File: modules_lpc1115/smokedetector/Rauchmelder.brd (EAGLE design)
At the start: 38 x 65 mm, 75 parts, among them IC1 BD9G101, IC2 LPC1115, Q1 BC856, Q3 BCP52, Q4 ASFL, T1 BC847C, T2 BC817

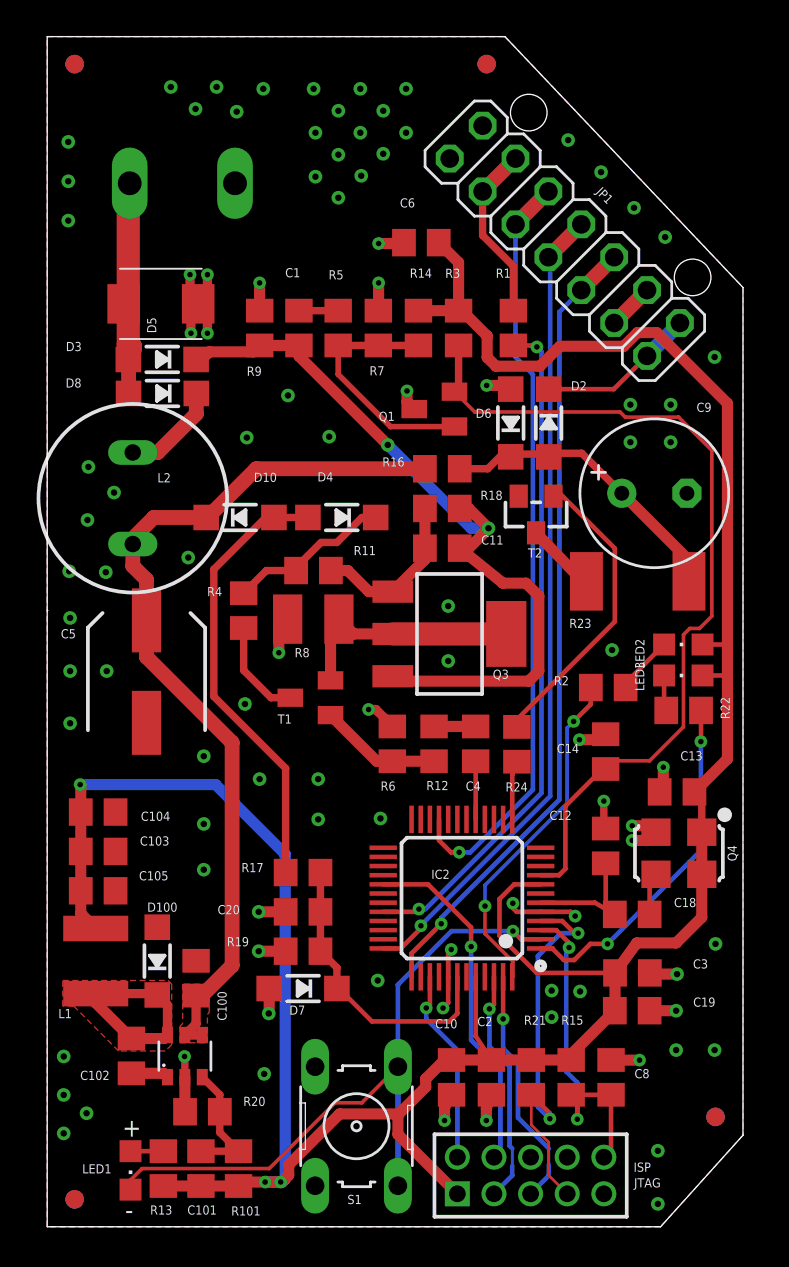
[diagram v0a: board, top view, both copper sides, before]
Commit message: [RM] - solved SWD connector collision with button
and optimized silk screen 
turned 330uF capacitor so that it is the same way rotated as in older PCB versions
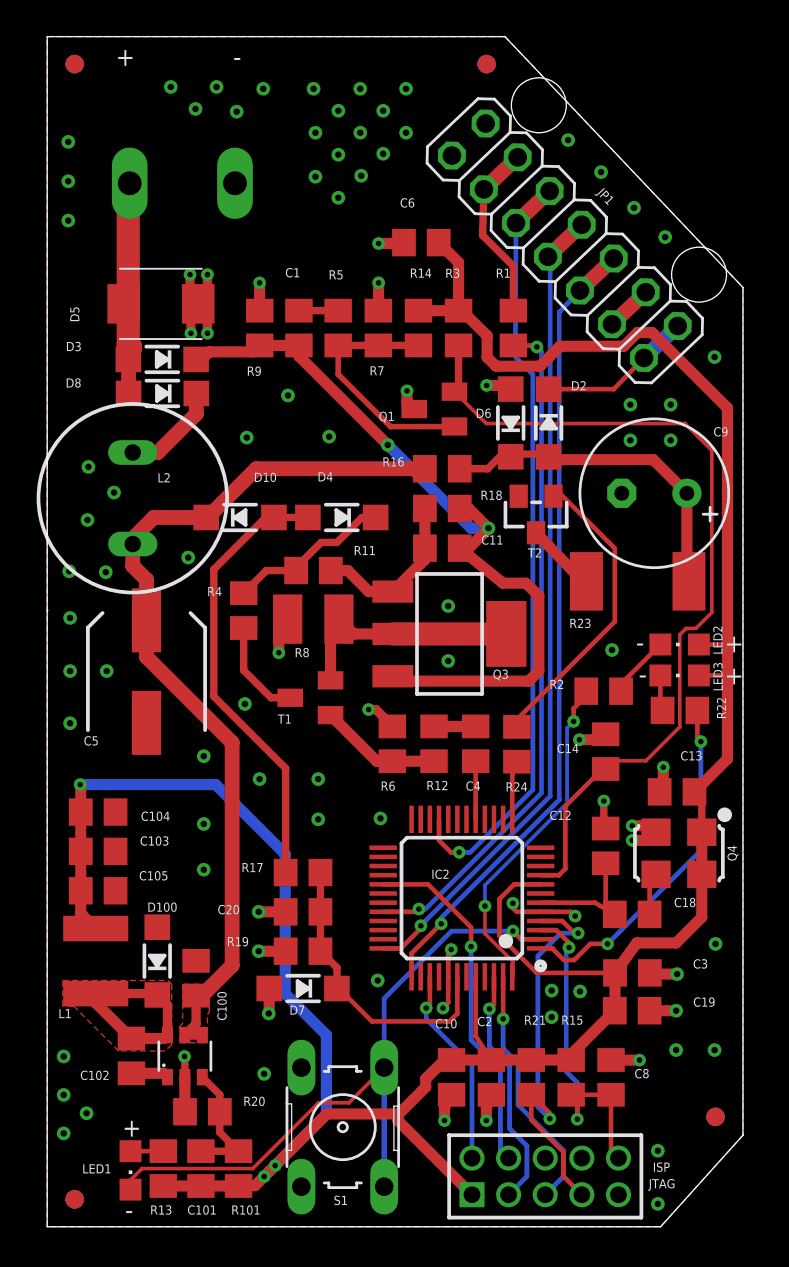
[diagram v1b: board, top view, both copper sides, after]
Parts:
- moved JTAG 0.80 mm to (27.2, 2.75)
- moved S1 0.75 mm to (16.1, 5.44)
- moved R2 0.32 mm to (30.4, 29.2)
- moved LED2 0.20 mm to (34.5, 31.8)
- moved LED3 0.20 mm to (34.5, 30.1)
- moved R22 0.20 mm to (34.6, 28.2)
- turned C9 to 180 degrees
- turned JP1 to 133.5 degrees
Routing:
- net N$10: track 16.7 -> 18.7 mm
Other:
- board text added: "Selfbus RM-ARM v3.8.4 RC2"
- board text removed: "Selfbus RM-ARM v3.8.4 RC1"

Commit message: [RM] -  smaller positioning changes; increased version
set version from 3.8.x to 3.9.x because of switch to 0805 which is a quite big change
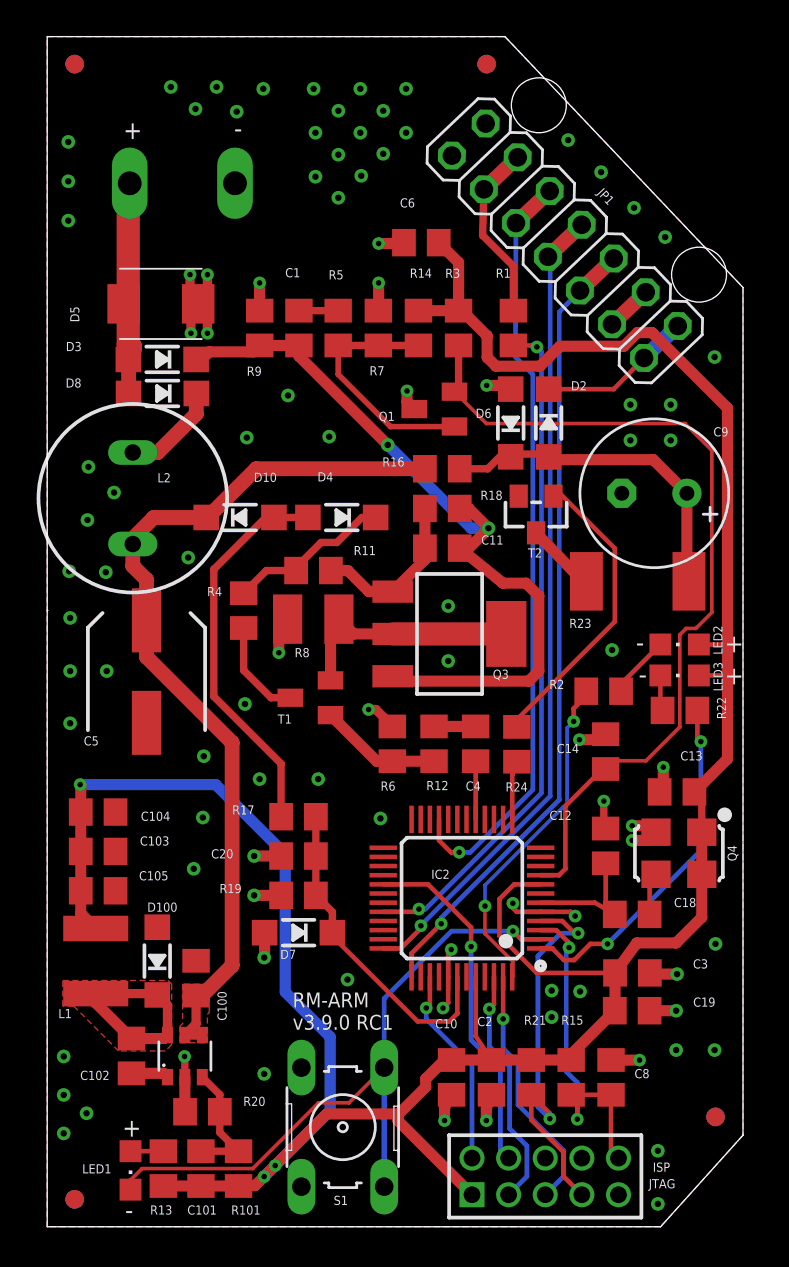
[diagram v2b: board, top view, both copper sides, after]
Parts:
- moved C20 3.06 mm to (13.7, 20.2)
- moved R17 3.06 mm to (13.7, 22.4)
- moved D7 3.06 mm to (13.7, 16.1)
- moved R19 3.06 mm to (13.7, 18.1)
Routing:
- net REF: track 24.5 -> 21.3 mm
- net BUS_V1: track 16.2 -> 17.8 mm
- net GND: vias 97 -> 96
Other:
- board text added: "RM-ARM v3.9.0 RC1"
- board text added: "Selfbus RM-ARM v3.9.0 RC1"
- board text removed: "Selfbus RM-ARM v3.8.4 RC2"

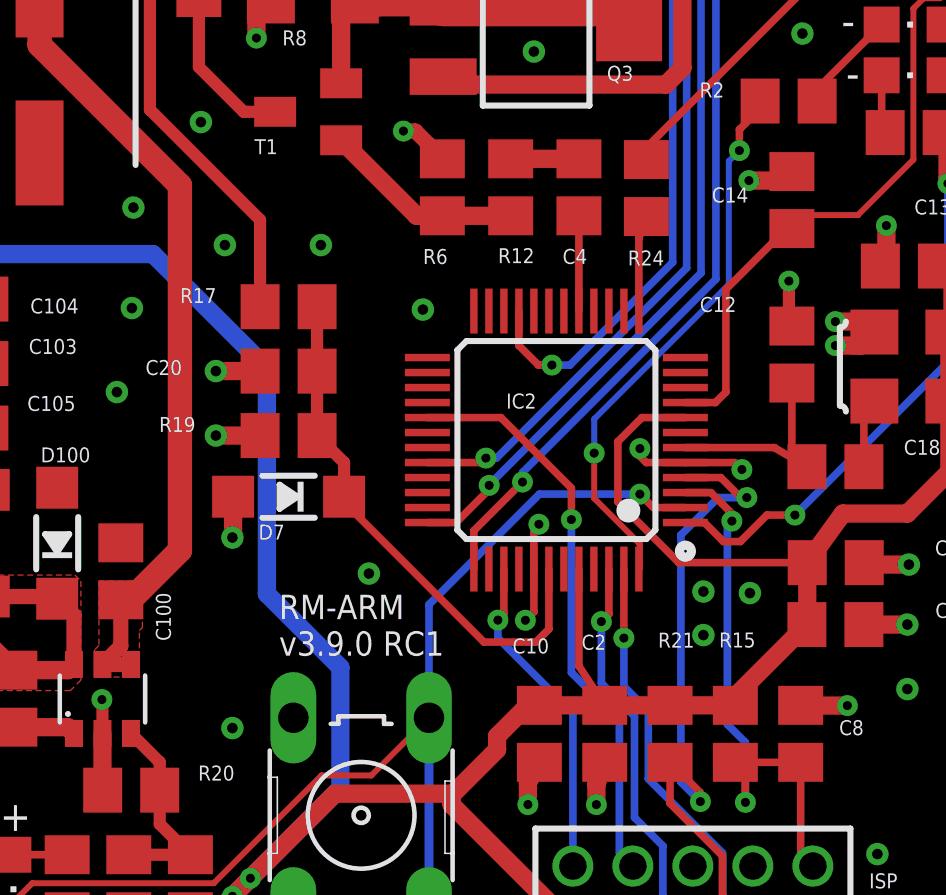
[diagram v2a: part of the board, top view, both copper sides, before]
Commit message: [RM] - corrected wrong part for C102 and error in solder topcoat
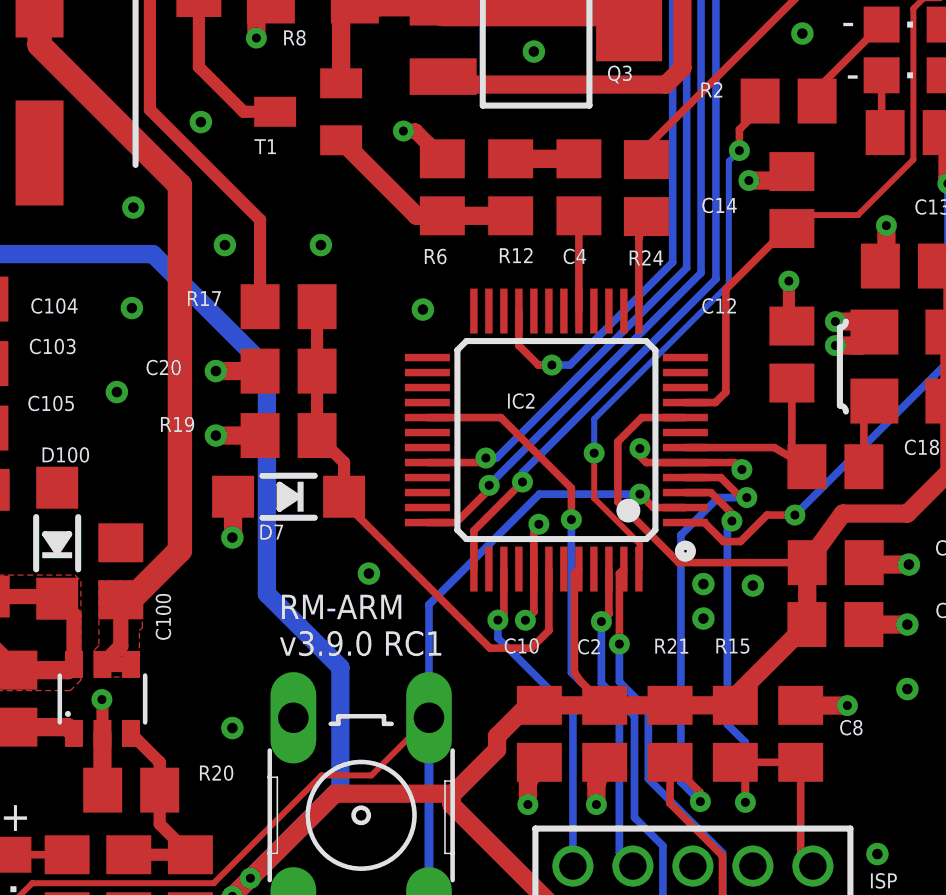
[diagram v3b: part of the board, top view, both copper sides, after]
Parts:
- C102: device rcl:R0805 -> rcl:C0805

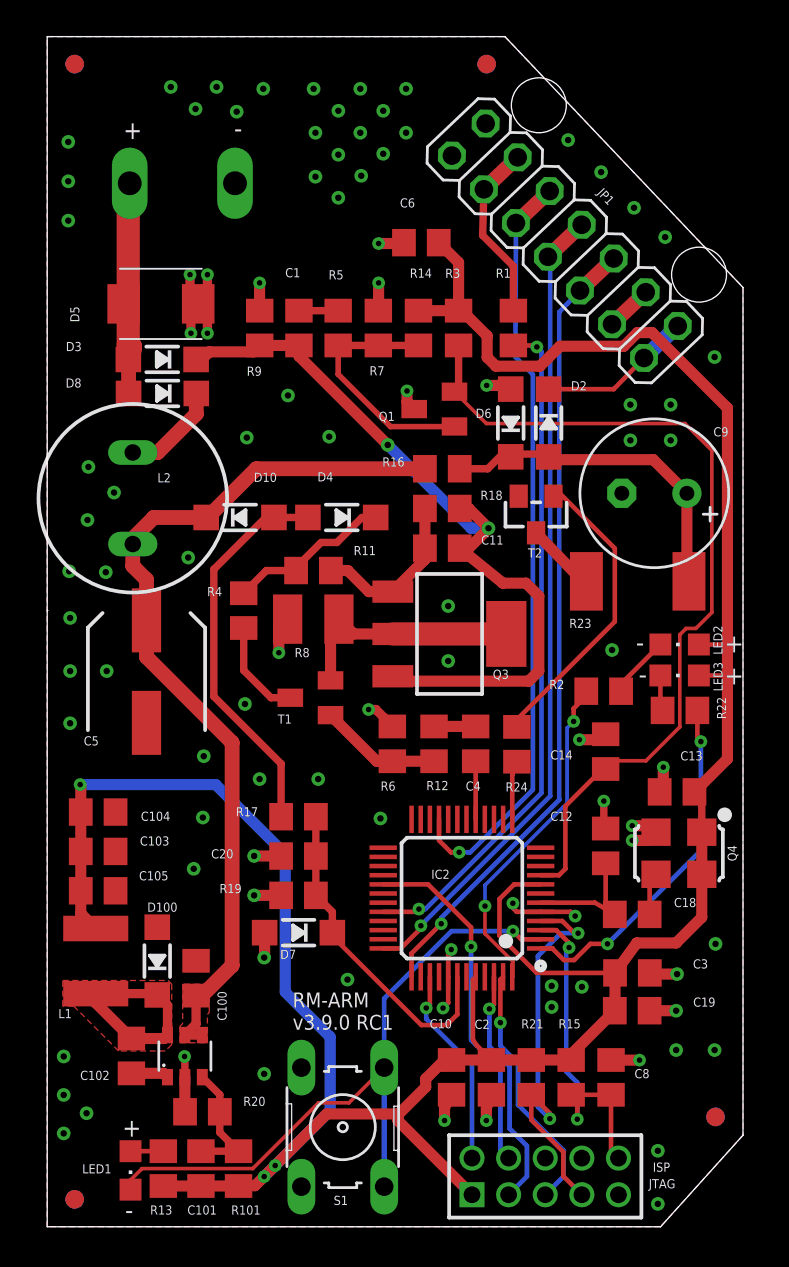
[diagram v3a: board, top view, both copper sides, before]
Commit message: [RM] - optimized silk screen; renamed pwr parts to correspond ARM TS
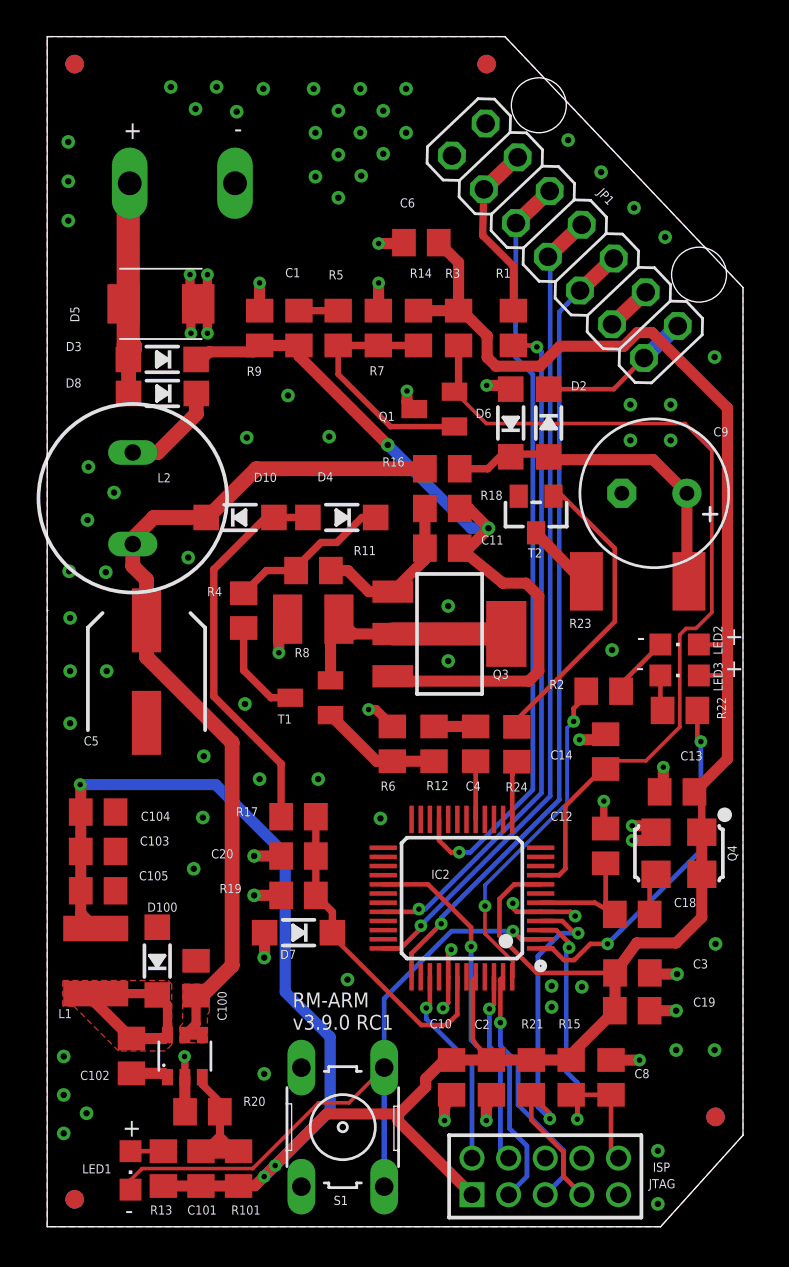
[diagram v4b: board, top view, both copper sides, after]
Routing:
- net FB1: track 6.92 -> 9.76 mm
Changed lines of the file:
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@@
 <text x="4.1512" y="59.403575" size="1" layer="21" ratio="10">+</text>
 <text x="10.2012" y="59.495575" size="1.016" layer="21" ratio="10">-</text>
-<text x="37.0012" y="31.370575" size="1" layer="21" ratio="10">+</text>
-<text x="37.0012" y="29.620575" size="1" layer="21" ratio="10">+</text>
-<text x="32.1512" y="31.420575" size="1.016" layer="21" ratio="10">-</text>
-<text x="32.3012" y="29.670575" size="1.016" layer="21" ratio="10">-</text>
+<text x="37.0012" y="31.770575" size="1" layer="21" ratio="10">+</text>
+<text x="37.0012" y="30.020575" size="1" layer="21" ratio="10">+</text>
+<text x="32.2012" y="31.720575" size="1.016" layer="21" ratio="10">-</text>
+<text x="32.1512" y="30.070575" size="1.016" layer="21" ratio="10">-</text>
 <text x="13.404375" y="10.7619" size="0.8128" layer="21" ratio="7">RM-ARM
 v3.9.0 RC1</text>
@@
 <contactref element="R20" pad="2"/>
 <contactref element="R101" pad="1"/>
-<wire x1="8.469" y1="8.17" x2="9.427" y2="7.212" width="0.4064" layer="1"/>
-<wire x1="9.427" y1="7.212" x2="9.427" y2="6.28" width="0.4064" layer="1"/>
-<wire x1="8.396" y1="4.1274125" x2="10.45" y2="4.1274125" width="0.4064" layer="1"/>
-<wire x1="10.45" y1="4.1274125" x2="9.427" y2="5.1504125" width="0.4064" layer="1"/>
-<wire x1="9.427" y1="5.1504125" x2="9.427" y2="6.28" width="0.4064" layer="1"/>
+<wire x1="9.427" y1="6.812" x2="8.469" y2="7.77" width="0.4064" layer="1"/>
+<wire x1="8.469" y1="8.17" x2="8.469" y2="7.77" width="0.4064" layer="1"/>
+<wire x1="9.427" y1="6.812" x2="9.427" y2="6.28" width="0.4064" layer="1"/>
+<wire x1="10.35" y1="4.2274125" x2="8.496" y2="4.2274125" width="1.016" layer="1"/>
+<wire x1="8.396" y1="4.1274125" x2="8.496" y2="4.2274125" width="1.016" layer="1"/>
+<wire x1="10.35" y1="4.2274125" x2="10.45" y2="4.1274125" width="1.016" layer="1"/>
+<wire x1="10.45" y1="4.1274125" x2="10.3" y2="4.1274125" width="0.4064" layer="1"/>
+<wire x1="10.3" y1="4.1274125" x2="9.427" y2="5.0004125" width="0.4064" layer="1"/>
+<wire x1="9.427" y1="5.0004125" x2="9.427" y2="6.28" width="0.4064" layer="1"/>
+<wire x1="9.427" y1="6.28" x2="9.427" y2="5.0084125" width="0.4064" layer="1"/>
+<wire x1="9.427" y1="5.0084125" x2="8.546" y2="4.1274125" width="0.4064" layer="1"/>
+<wire x1="8.546" y1="4.1274125" x2="8.396" y2="4.1274125" width="0.4064" layer="1"/>
 </signal>
 <signal name="+3V3">
